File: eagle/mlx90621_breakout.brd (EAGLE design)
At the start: 53.3 x 59.7 mm, 12 parts

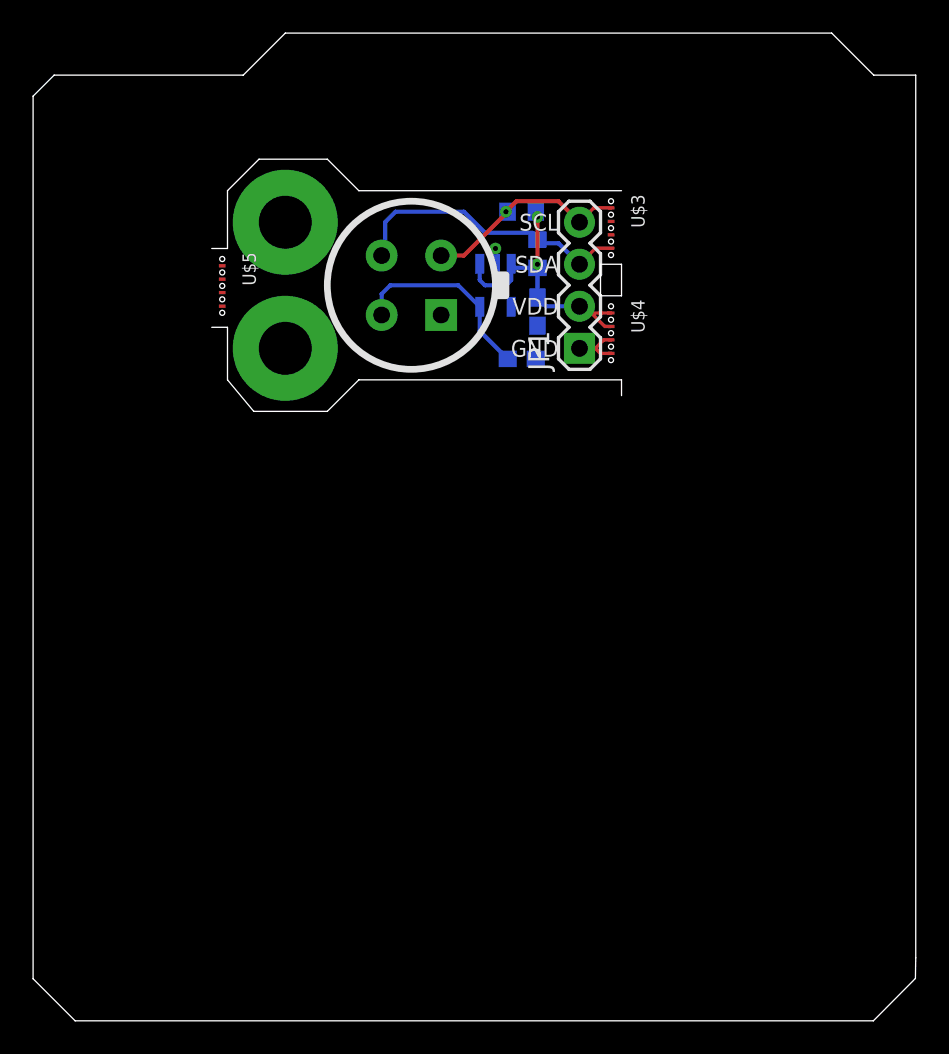
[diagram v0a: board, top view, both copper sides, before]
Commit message: added measures and cleaned the board for clearer look
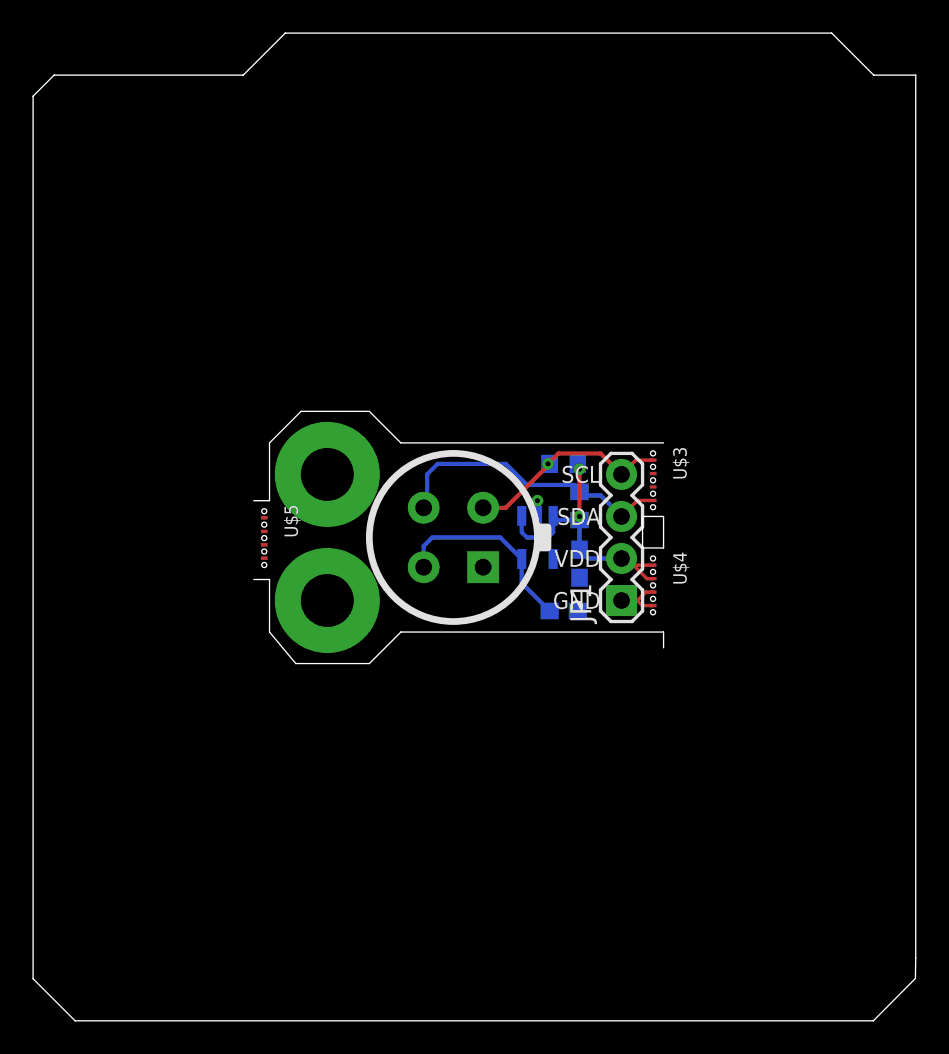
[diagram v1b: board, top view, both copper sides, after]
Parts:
- moved C2 15.5 mm to (32.1, 24.8)
- moved R1 15.5 mm to (32.1, 33.7)
- moved S1 15.5 mm to (17.8, 25.4)
- moved U$3 15.5 mm to (37.5, 34.3)
- moved U$5 15.5 mm to (14.0, 30.8)
- moved C1 15.5 mm to (33.0, 27.6)
- moved JP1 15.5 mm to (35.6, 25.4)
- moved R2 15.5 mm to (33.0, 31.1)
- moved U$1 15.5 mm to (25.4, 29.2)
- moved U$2 15.5 mm to (30.5, 29.2)
- moved U$4 15.5 mm to (37.5, 27.9)
- moved S2 15.5 mm to (17.8, 33.0)
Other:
- outline, holes or cut-outs redrawn
